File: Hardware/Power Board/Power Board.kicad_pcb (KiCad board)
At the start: 2 copper layers, 179 x 179 mm, 63 parts, among them J1 Conn_02x09_Counter_Clockwise, J10 Conn_01x05_MountingPin, J2 Conn_02x09_Counter_Clockwise, J3 Conn_02x09_Counter_Clockwise, J4 Conn_01x05_MountingPin, J5 Conn_01x05_MountingPin, J6 Conn_01x05_MountingPin, J7 Conn_01x05_MountingPin, J8 Conn_01x05_MountingPin, J9 Conn_01x05_MountingPin

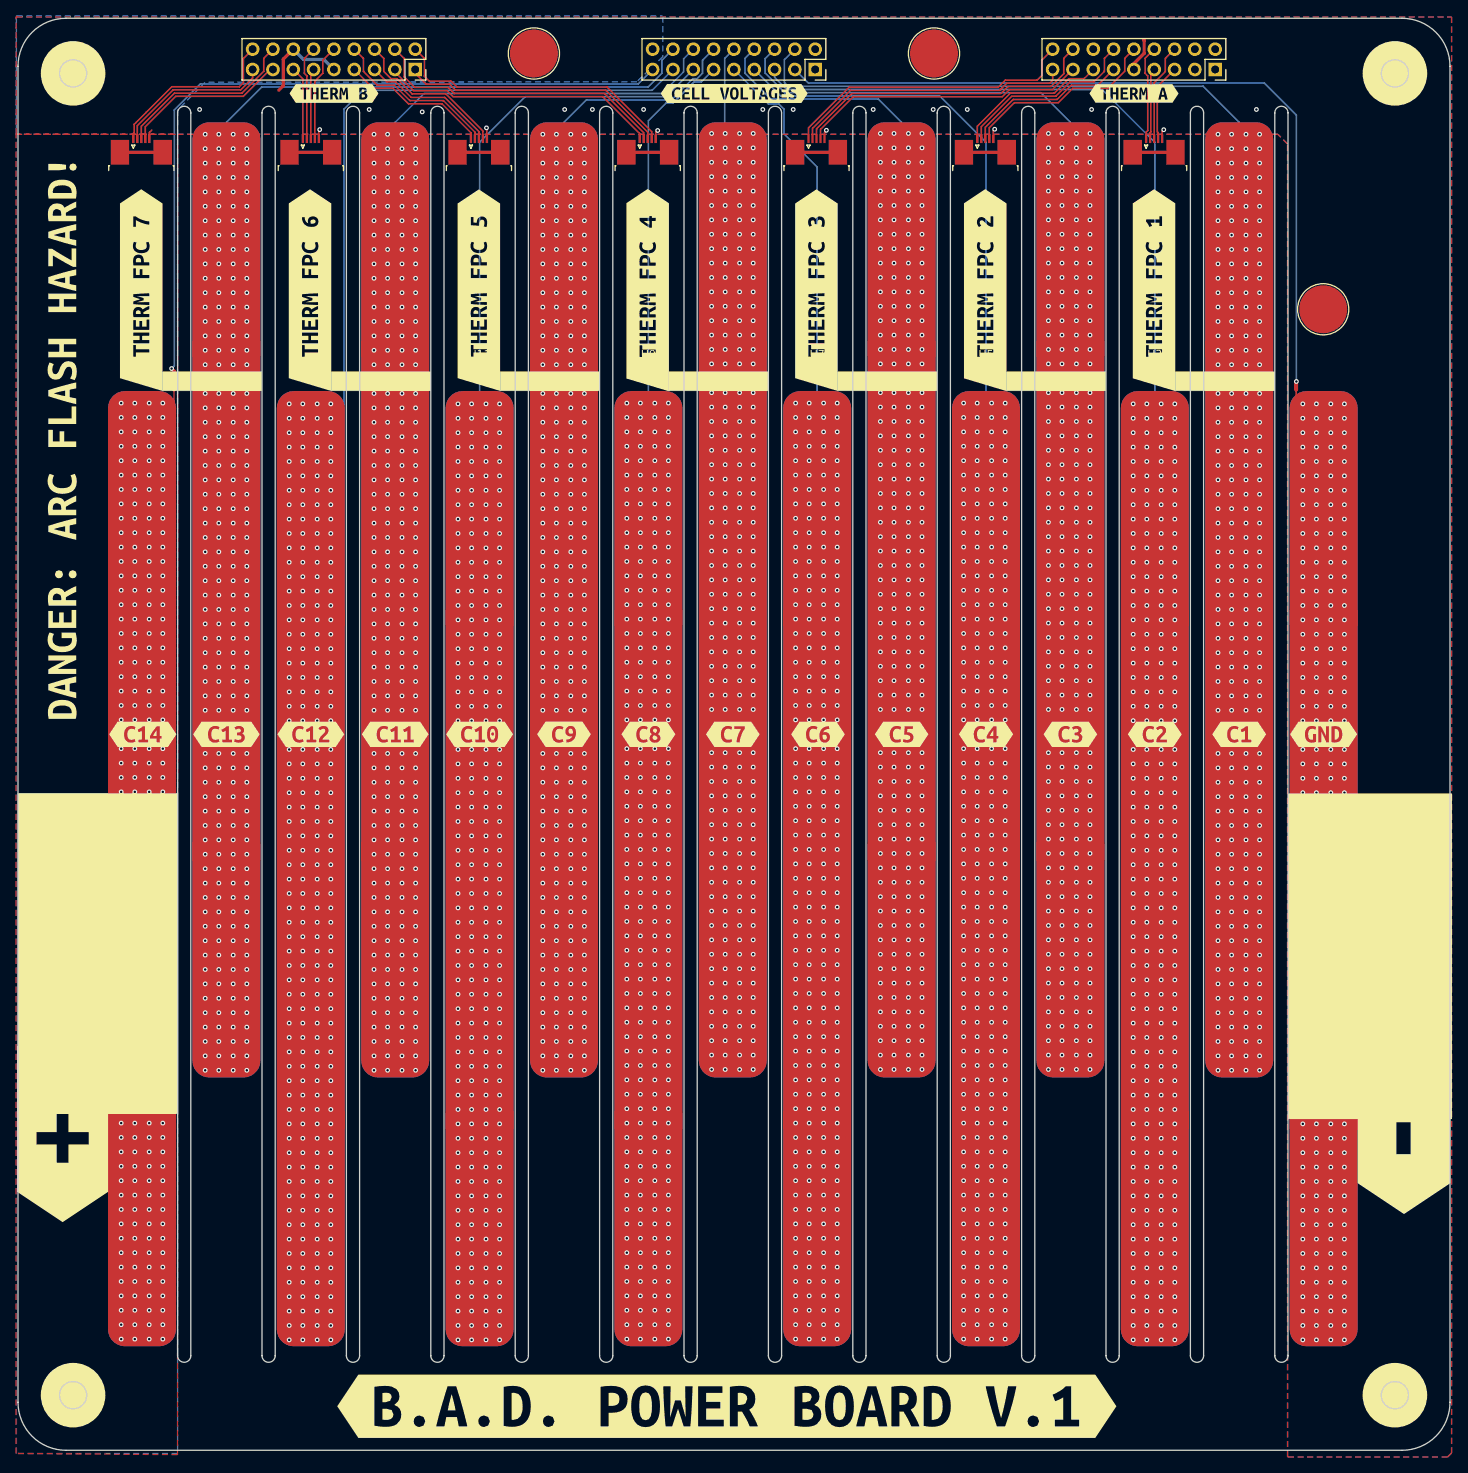
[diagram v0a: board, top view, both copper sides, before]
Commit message: BMS updates, power/fet final updates
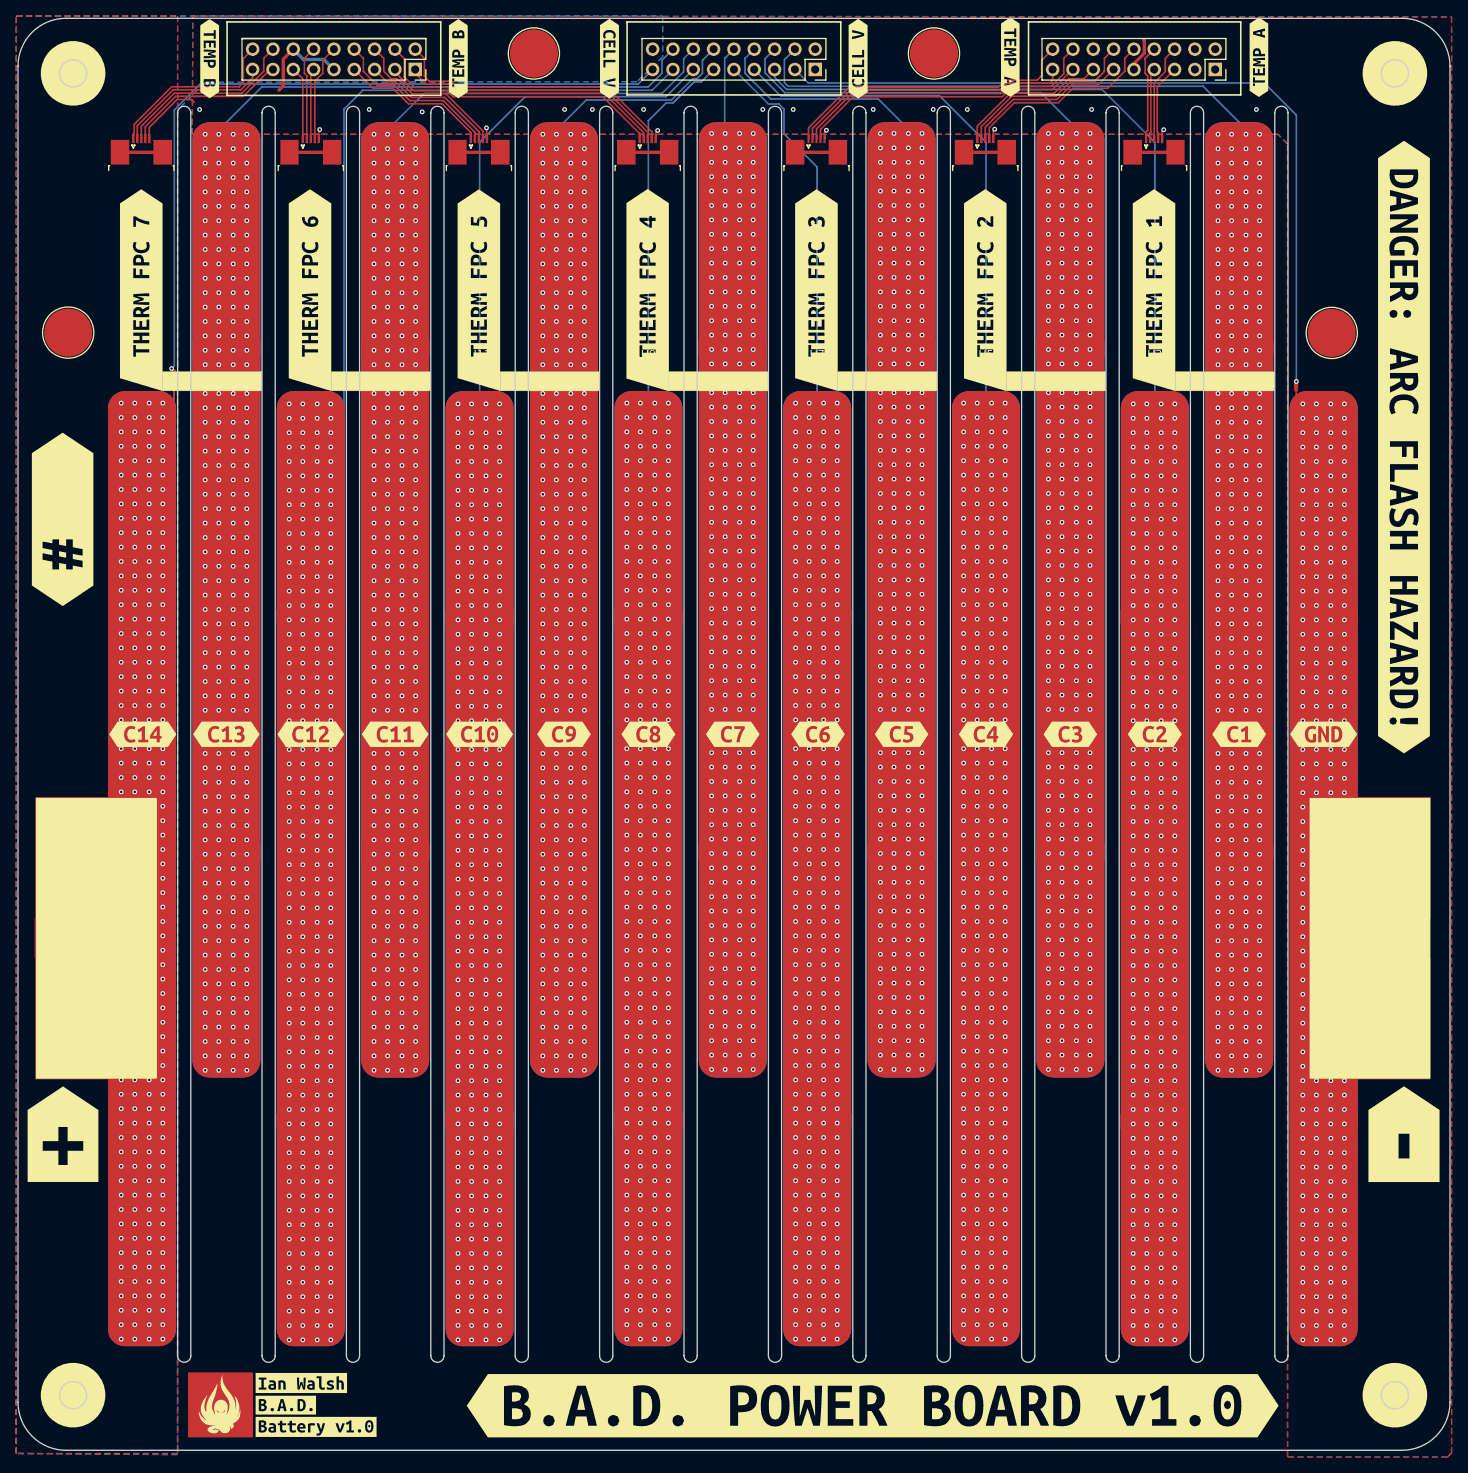
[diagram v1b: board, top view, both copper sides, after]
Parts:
- removed kibuzzard-68FE8B33: G***, kibuzzard-68FE8B33
- removed kibuzzard-68FE9694: G***, kibuzzard-68FE9694
- removed kibuzzard-68FE96E6: G***, kibuzzard-68FE96E6
- removed kibuzzard-68FE9708: G***, kibuzzard-68FE9708
- removed kibuzzard-68FE9876: G***, kibuzzard-68FE9876
- removed kibuzzard-68FE9A02: G***, kibuzzard-68FE9A02
- removed kibuzzard-68FEE0E1: G***, kibuzzard-68FEE0E1
- added G*** (x2): LOGO, LOGO, F.Cu at (99.8, 216.9)
- added G***: LOGO, LOGO, B.Cu at (163.9, 138.4)
- added REF**: TestPoint_Pad_D4.0mm, TestPoint:TestPoint_Pad_D4.0mm, F.Cu at (80.8, 82.9)
- added kibuzzard-69080430: G***, kibuzzard-69080430, F.Cu at (109.9, 214.2)
- added kibuzzard-69080435: G***, kibuzzard-69080435, F.Cu at (108.0, 217.0)
- added kibuzzard-6908043A: G***, kibuzzard-6908043A, F.Cu at (111.8, 219.7)
- added kibuzzard-690804B6: G***, kibuzzard-690804B6, F.Cu at (181.3, 217.0)
- added kibuzzard-69080668: G***, kibuzzard-69080668, F.Cu at (247.7, 97.2)
- added kibuzzard-69080D2C: G***, kibuzzard-69080D2C, F.Cu at (148.4, 48.6)
- added kibuzzard-69080D2C: G***, kibuzzard-69080D2C, F.Cu at (179.5, 48.6)
- added kibuzzard-69080D5F: G***, kibuzzard-69080D5F, F.Cu at (129.5, 48.6)
- added kibuzzard-69080D67: G***, kibuzzard-69080D67, F.Cu at (98.5, 48.6)
- added kibuzzard-69080DC3: G***, kibuzzard-69080DC3, F.Cu at (198.5, 48.5)
- added kibuzzard-69080DCA: G***, kibuzzard-69080DCA, F.Cu at (229.6, 48.5)
- added kibuzzard-690816F8: G***, kibuzzard-690816F8, F.Cu at (80.1, 106.2)
- added kibuzzard-69081DDA: G***, kibuzzard-69081DDA, F.Cu at (247.8, 183.1)
- added kibuzzard-69081DE1: G***, kibuzzard-69081DE1, F.Cu at (80.1, 183.1)
- moved REF** 3.14 mm to (238.7, 82.9)
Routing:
- net GND: track 42.6 -> 50.0 mm
- added copper zone on In1.Cu, net /CELL_14
- added copper zone on In2.Cu, net /CELL_14
- added copper zone on In1.Cu, net GND
- added copper zone on In2.Cu, net GND
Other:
- copper layers 2 -> 4

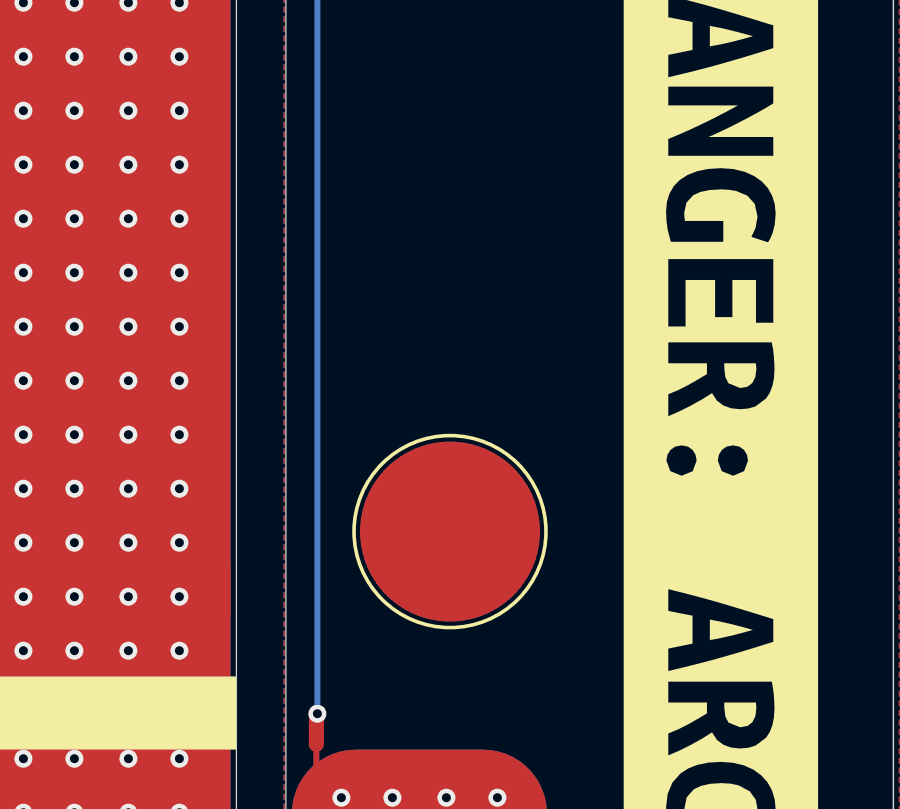
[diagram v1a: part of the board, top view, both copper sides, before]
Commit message: fab updates to bms, power board, fet board
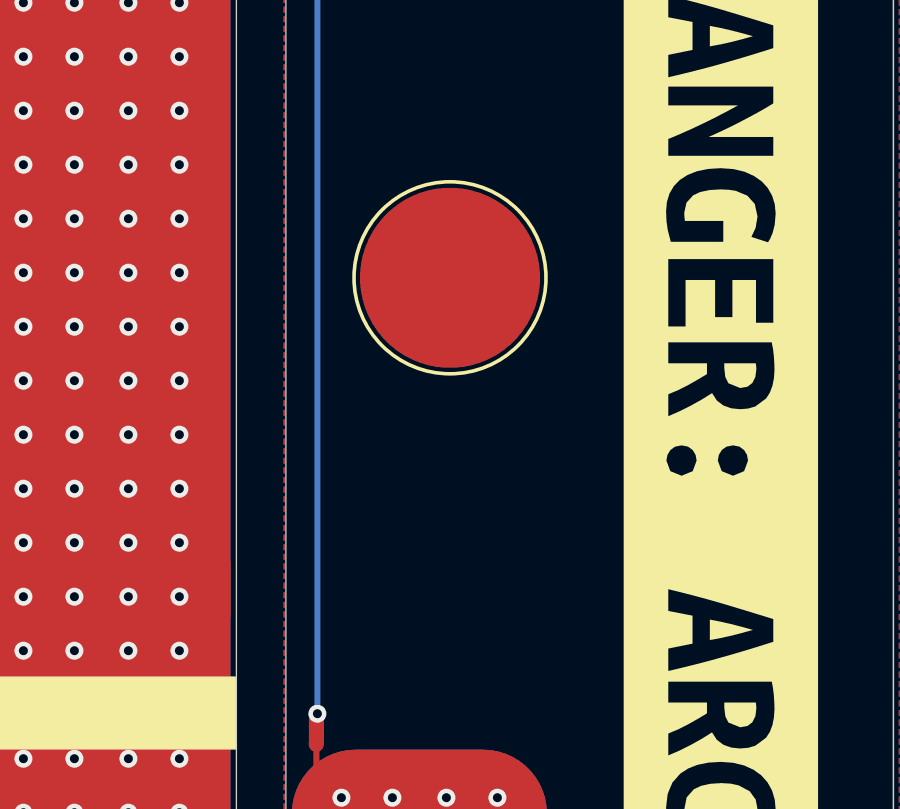
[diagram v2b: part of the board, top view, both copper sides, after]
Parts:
- moved REF** 8.46 mm to (238.7, 74.5)
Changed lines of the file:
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@@
 	(footprint "TestPoint:TestPoint_Pad_D4.0mm"
 		(layer "F.Cu")
-		(at 238.72 82.93)
+		(at 238.72 74.47)
 		(descr "SMD pad as test Point, diameter 4.0mm")
 		(tags "test point SMD pad")
